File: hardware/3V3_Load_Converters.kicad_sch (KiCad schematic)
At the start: 73 parts, among them J23 61300311121, J24 61300311121, Q28 EPC2016C, Q29 EPC2016C, Q30 EPC2016C, Q31 EPC2016C, Q8 SI2302DDS-T1-GE3, Q9 SI2302DDS-T1-GE3, U21 INA199C3DCKR, U30 LTC3833EUDC-TRPBF, U31 LTC3833EUDC-TRPBF

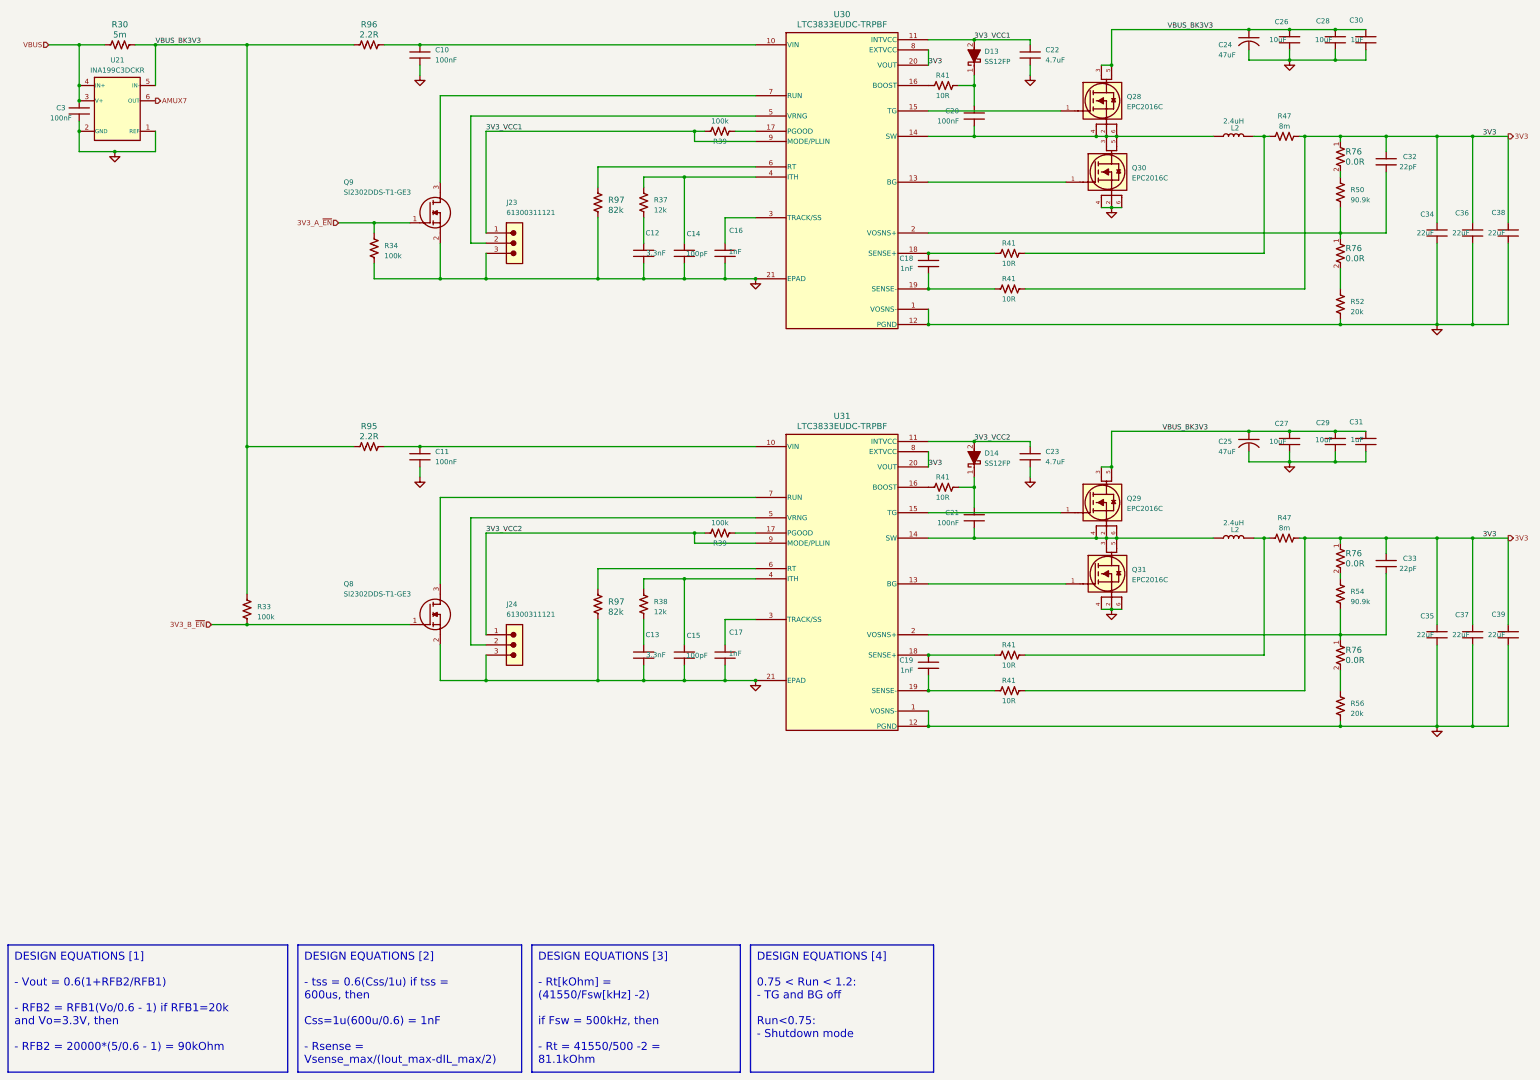
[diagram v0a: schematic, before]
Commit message: hardware: Updating the schematic and layout to solve #8, #9 and #10.
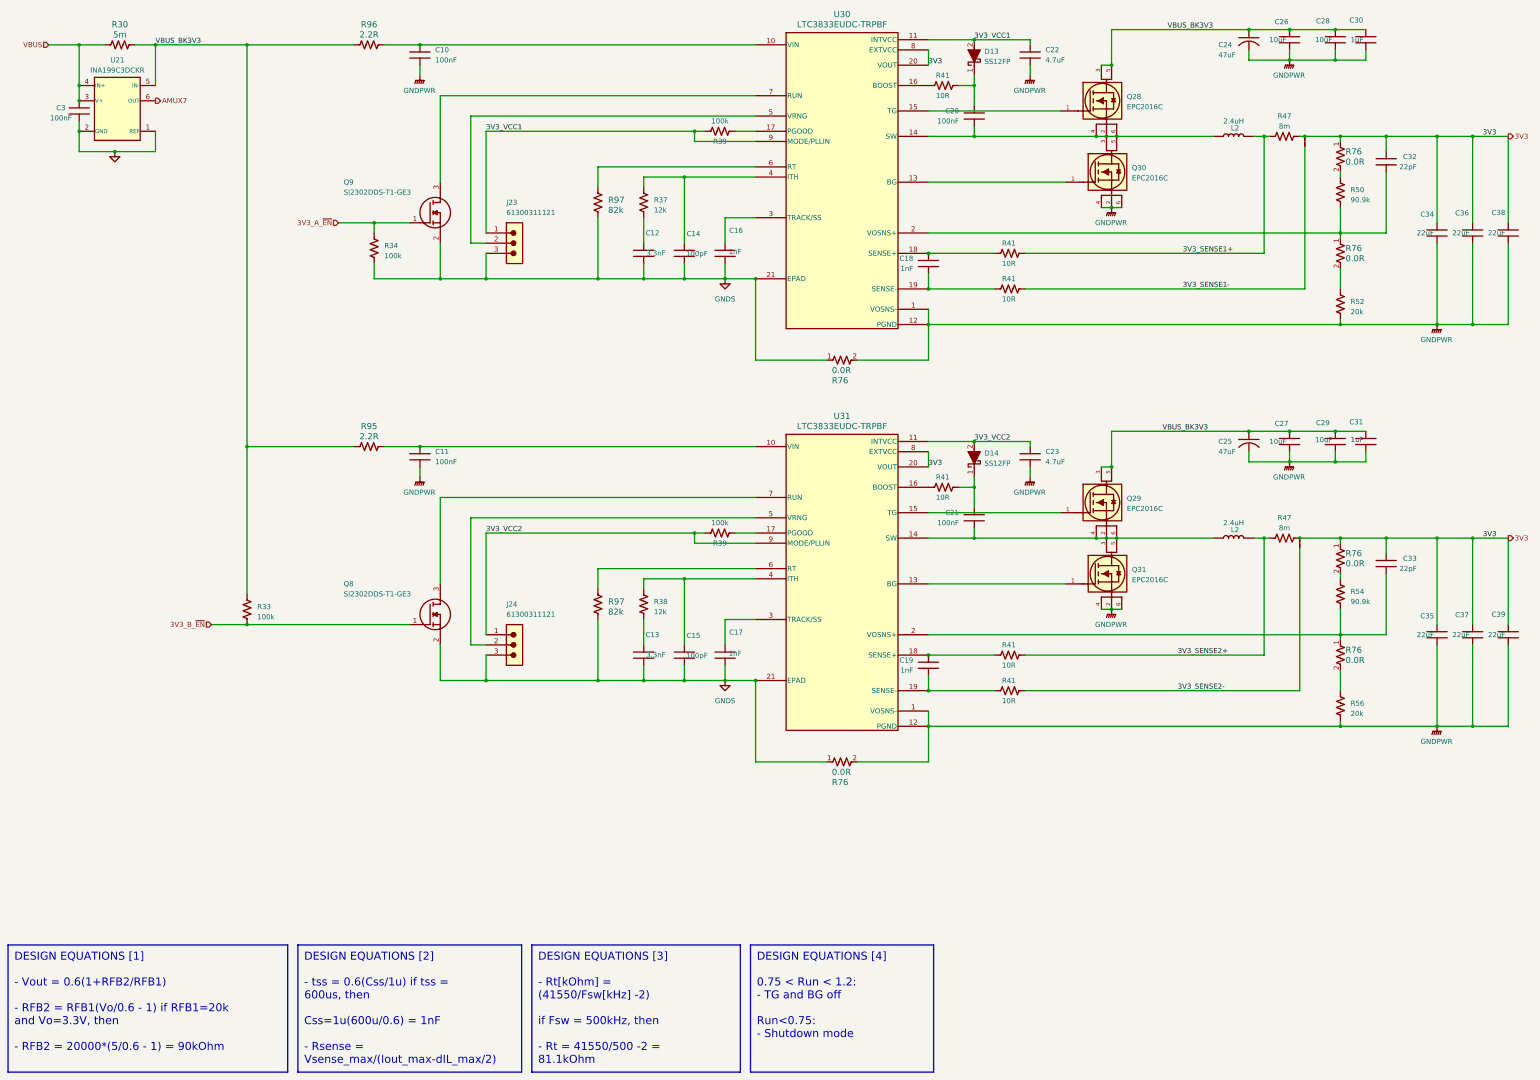
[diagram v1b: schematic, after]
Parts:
- added JP1, JP2: SolderJumper_2_Bridged, footprints:Jumper, symbol Jumper:Jumper
- added R76 (x2): 0.0R, footprints:CRCW06030000Z0EAHP, symbol CRCW06030000Z0EAHP:CRCW06030000Z0EAHP
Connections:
- net 3V3: now also JP1.2 (B), JP2.2 (B); no longer R41.1, R41.1
- net GND: no longer C10.1, C11.1, C12.2, C13.2, C14.2, C15.2, C16.2, C17.2, C22.2, C23.2, C24.1 (CATHODE), C25.1 (CATHODE), C26.2, C27.2, C28.2, C29.2, C30.2, C31.2, C34.1, C35.1, C36.1, C37.1, C38.1, C39.1, J23.3, J24.3, Q30.2 (Substrate), Q30.4 (Source), Q30.6 (Source), Q31.2 (Substrate), Q31.4 (Source), Q31.6 (Source), Q8.2 (S), Q9.2 (S), R34.1, R52.1, R56.1, R97.1, R97.1, U30.1 (VOSNS-), U30.12 (PGND), U30.21 (EPAD), U31.1 (VOSNS-), U31.12 (PGND), U31.21 (EPAD)
- net 3V3_SENSE2+: now reaches L2.2, R41.1, R47.2
- net 3V3_SENSE1+: now reaches L2.2, R41.1, R47.2
- new net 3V3_SENSE1-: JP2.1 (A), R41.1
- new net 3V3_SENSE2-: JP1.1 (A), R41.1
- new net GNDPWR: C10.1, C11.1, C22.2, C23.2, C24.1 (CATHODE), C25.1 (CATHODE), C26.2, C27.2, C28.2, C29.2, C30.2, C31.2, C34.1, C35.1, C36.1, C37.1, C38.1, C39.1, Q30.2 (Substrate), Q30.4 (Source), Q30.6 (Source), Q31.2 (Substrate), Q31.4 (Source), Q31.6 (Source), R52.1, R56.1, R76.2, R76.2, U30.1 (VOSNS-), U30.12 (PGND), U31.1 (VOSNS-), U31.12 (PGND)
- new net GNDS: C12.2, C13.2, C14.2, C15.2, C16.2, C17.2, J23.3, J24.3, Q8.2 (S), Q9.2 (S), R34.1, R76.1, R76.1, R97.1, R97.1, U30.21 (EPAD), U31.21 (EPAD)

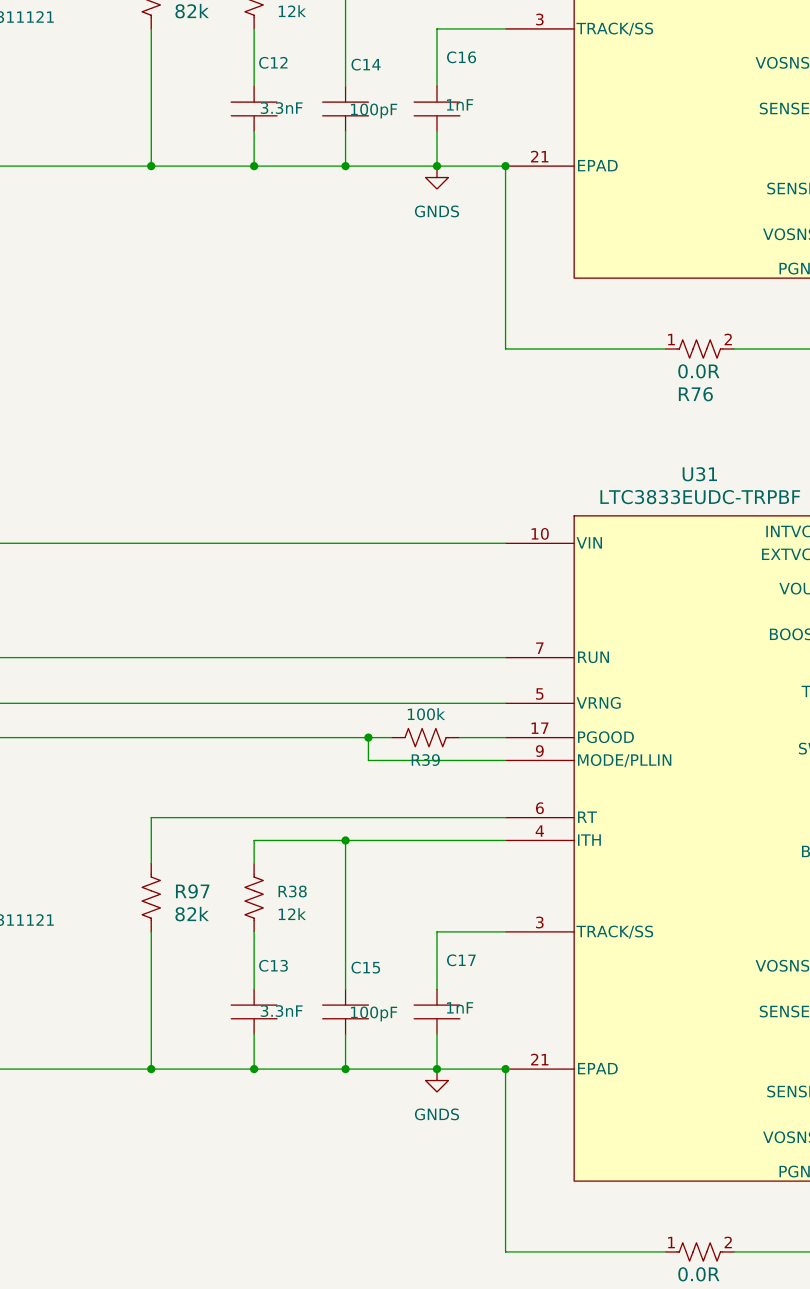
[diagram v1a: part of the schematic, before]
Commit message: hardware: Making corrections regarding #15, #14, #13 and starting #12 and #11.
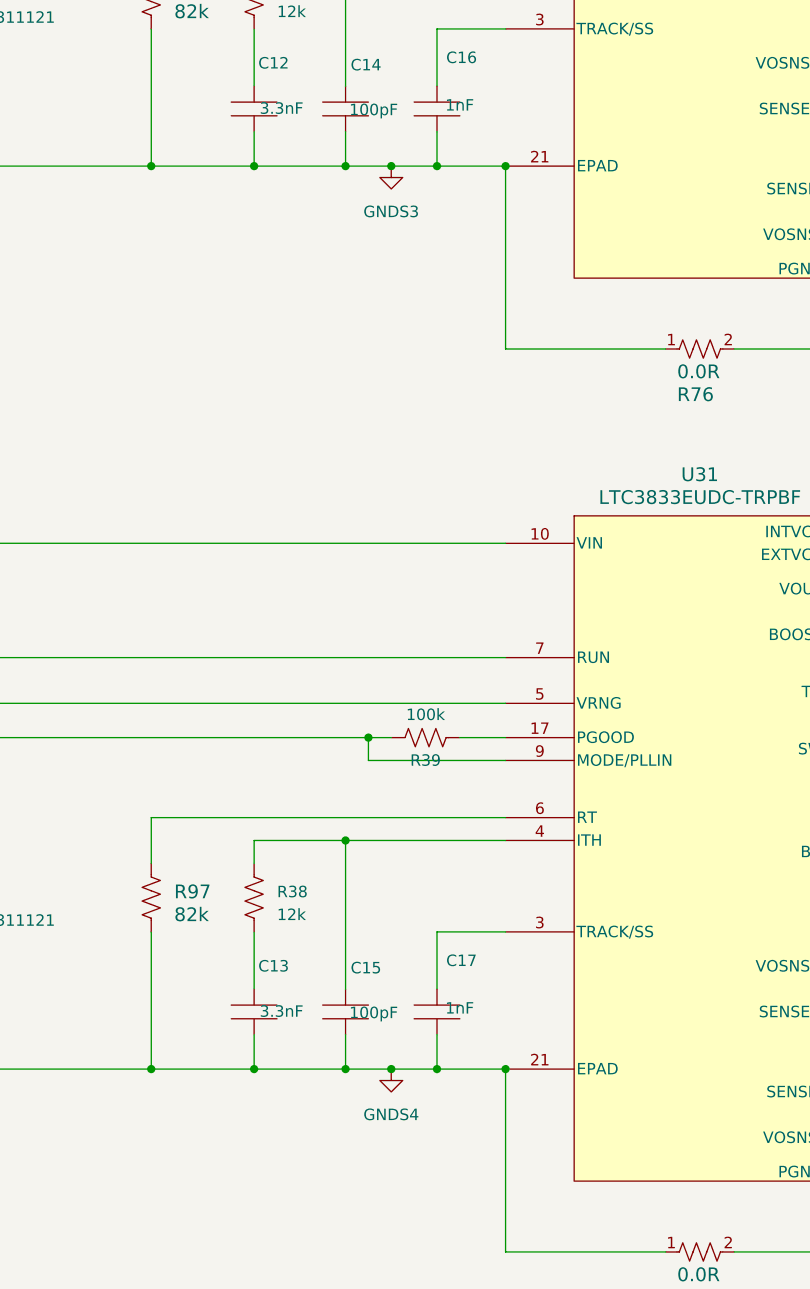
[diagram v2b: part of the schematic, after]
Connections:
- net GNDS renamed GNDS3
- net GNDS3: no longer C13.2, C15.2, C17.2, J24.3, Q8.2 (S), R76.1, R97.1, U31.21 (EPAD)
- new net GNDS4: C13.2, C15.2, C17.2, J24.3, Q8.2 (S), R76.1, R97.1, U31.21 (EPAD)
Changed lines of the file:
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@@
   (junction (at 106.68 69.85) (diameter 0) (color 0 0 0 0)
   )
+  (junction (at 189.23 83.82) (diameter 0) (color 0 0 0 0)
+  )
   (junction (at 359.41 148.59) (diameter 0) (color 0 0 0 0)
   )
@@
   (junction (at 184.15 184.15) (diameter 0) (color 0 0 0 0)
   )
+  (junction (at 189.23 184.15) (diameter 0) (color 0 0 0 0)
+  )
   (junction (at 245.11 186.69) (diameter 0) (color 0 0 0 0)
   )
@@
     (stroke (width 0) (type default))
   )
+  (wire (pts (xy 189.23 83.82) (xy 194.31 83.82))
+    (stroke (width 0) (type default))
+  )
   (wire (pts (xy 194.31 184.15) (xy 201.93 184.15))
     (stroke (width 0) (type default))
@@
     (stroke (width 0) (type default))
   )
+  (wire (pts (xy 189.23 184.15) (xy 194.31 184.15))
+    (stroke (width 0) (type default))
+  )
   (wire (pts (xy 186.69 46.99) (xy 189.23 46.99))
     (stroke (width 0) (type default))
@@
     (stroke (width 1) (type default))
   )
-  (wire (pts (xy 184.15 184.15) (xy 194.31 184.15))
-    (stroke (width 0) (type default))
-  )
   (wire (pts (xy 335.28 121.92) (xy 346.71 121.92))
     (stroke (width 1) (type default))
@@
     (stroke (width 0) (type default))
   )
+  (wire (pts (xy 184.15 184.15) (xy 189.23 184.15))
+    (stroke (width 0) (type default))
+  )
   (wire (pts (xy 354.33 26.67) (xy 354.33 29.21))
     (stroke (width 0) (type default))
@@
     (stroke (width 0) (type default))
   )
-  (wire (pts (xy 184.15 83.82) (xy 194.31 83.82))
+  (wire (pts (xy 184.15 83.82) (xy 189.23 83.82))
     (stroke (width 0) (type default))
   )
@@
         (path "/2eebaa11-d7ed-4bfd-bc8e-988f68654d29/6f34948c-43a8-4614-b8ed-90c5b6b9b243"
           (reference "R98") (unit 1)
-        )
-      )
-    )
-  )
-  (symbol (lib_id "power:GNDS") (at 194.31 184.15 0) (unit 1)
-    (in_bom yes) (on_board yes) (dnp no) (fields_autoplaced)
-    (property "Reference" "#PWR055" (at 194.31 190.5 0)
-      (effects (font (size 1.27 1.27)) hide)
-    )
-    (property "Value" "GNDS" (at 194.31 189.23 0)
-      (effects (font (size 1.27 1.27)))
-    )
-    (property "Footprint" "" (at 194.31 184.15 0)
-      (effects (font (size 1.27 1.27)) hide)
-    )
-    (property "Datasheet" "" (at 194.31 184.15 0)
-      (effects (font (size 1.27 1.27)) hide)
-    )
-    (pin "1")
-    (instances
-      (project "eps-re_project"
-        (path "/2eebaa11-d7ed-4bfd-bc8e-988f68654d29/6cd5fe02-9b19-49bf-9109-b0a2c2f10c14"
-          (reference "#PWR055") (unit 1)
-        )
-        (path "/2eebaa11-d7ed-4bfd-bc8e-988f68654d29/6f34948c-43a8-4614-b8ed-90c5b6b9b243"
-          (reference "#PWR060") (unit 1)
         )
       )
@@
     )
   )
+  (symbol (lib_id "GNDS4:GNDS4") (at 189.23 184.15 0) (unit 1)
+    (in_bom yes) (on_board yes) (dnp no) (fields_autoplaced)
+    (property "Reference" "#PWR060" (at 189.23 190.5 0)
+      (effects (font (size 1.27 1.27)) hide)
+    )
+    (property "Value" "GNDS4" (at 189.23 189.23 0)
+      (effects (font (size 1.27 1.27)))
+    )
+    (property "Footprint" "" (at 189.23 184.15 0)
+      (effects (font (size 1.27 1.27)) hide)
+    )
+    (property "Datasheet" "" (at 189.23 184.15 0)
+      (effects (font (size 1.27 1.27)) hide)
+    )
+    (pin "1")
+    (instances
+      (project "eps-re_project"
+        (path "/2eebaa11-d7ed-4bfd-bc8e-988f68654d29/6f34948c-43a8-4614-b8ed-90c5b6b9b243"
+          (reference "#PWR060") (unit 1)
+        )
+      )
+    )
+  )
   (symbol (lib_id "CRCW060310R0FKEAHP:CRCW060310R0FKEAHP") (at 257.556 135.89 180) (unit 1)
     (in_bom yes) (on_board yes) (dnp no)
@@
     )
   )
-  (symbol (lib_id "power:GNDS") (at 194.31 83.82 0) (unit 1)
+  (symbol (lib_id "GNDS3:GNDS3") (at 189.23 83.82 0) (unit 1)
     (in_bom yes) (on_board yes) (dnp no) (fields_autoplaced)
-    (property "Reference" "#PWR052" (at 194.31 90.17 0)
+    (property "Reference" "#PWR058" (at 189.23 90.17 0)
       (effects (font (size 1.27 1.27)) hide)
     )
-    (property "Value" "GNDS" (at 194.31 88.9 0)
+    (property "Value" "GNDS3" (at 189.23 88.9 0)
       (effects (font (size 1.27 1.27)))
     )
-    (property "Footprint" "" (at 194.31 83.82 0)
+    (property "Footprint" "" (at 189.23 83.82 0)
       (effects (font (size 1.27 1.27)) hide)
     )
-    (property "Datasheet" "" (at 194.31 83.82 0)
+    (property "Datasheet" "" (at 189.23 83.82 0)
       (effects (font (size 1.27 1.27)) hide)
     )
@@
     (instances
       (project "eps-re_project"
-        (path "/2eebaa11-d7ed-4bfd-bc8e-988f68654d29/6cd5fe02-9b19-49bf-9109-b0a2c2f10c14"
-          (reference "#PWR052") (unit 1)
-        )
         (path "/2eebaa11-d7ed-4bfd-bc8e-988f68654d29/6f34948c-43a8-4614-b8ed-90c5b6b9b243"
           (reference "#PWR058") (unit 1)
